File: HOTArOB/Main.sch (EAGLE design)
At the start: 15 parts

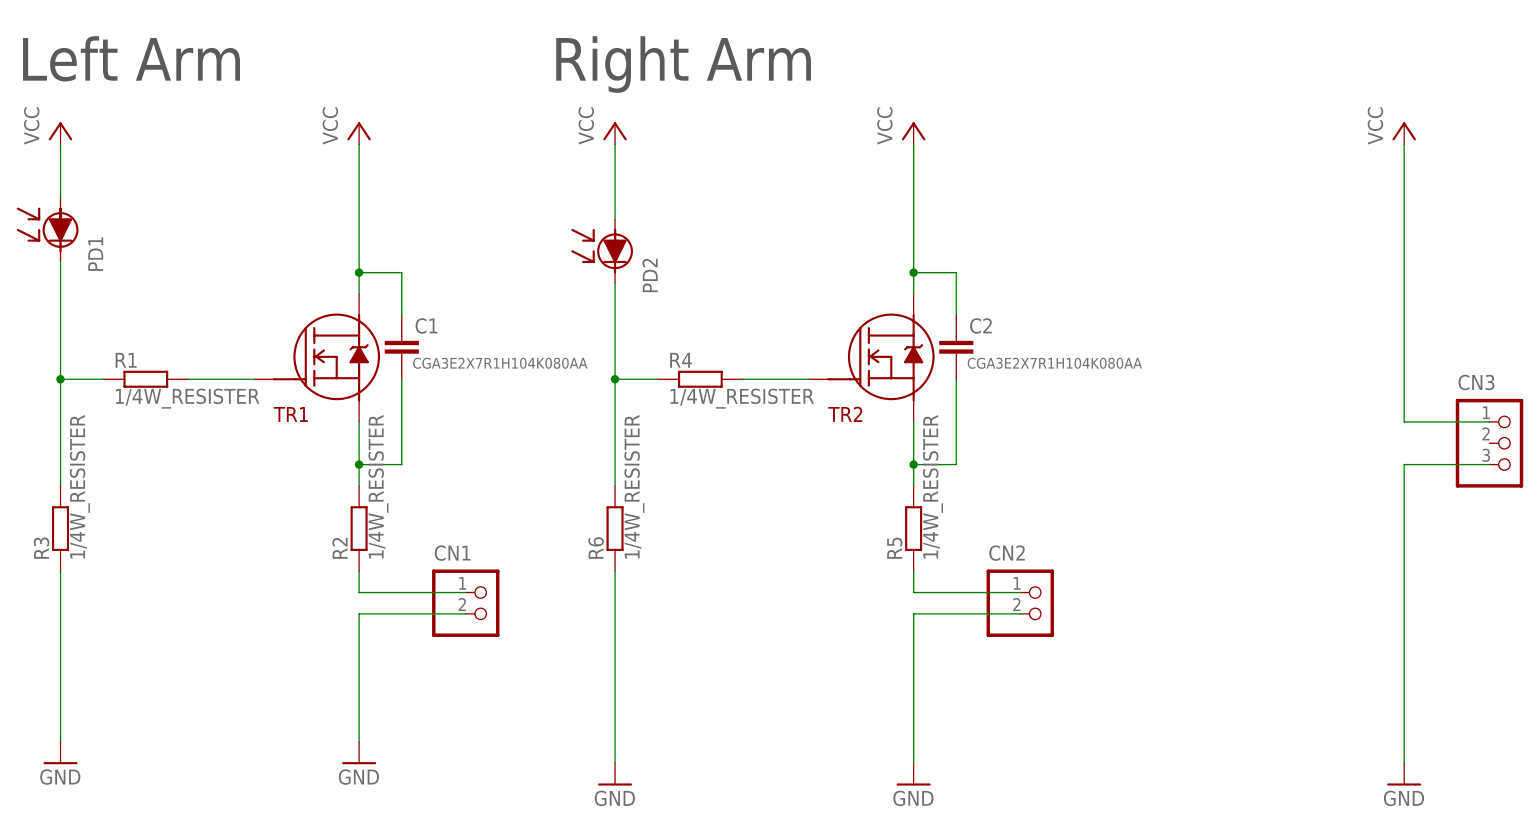
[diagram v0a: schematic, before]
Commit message: Change sensor
Photo diode to CdS
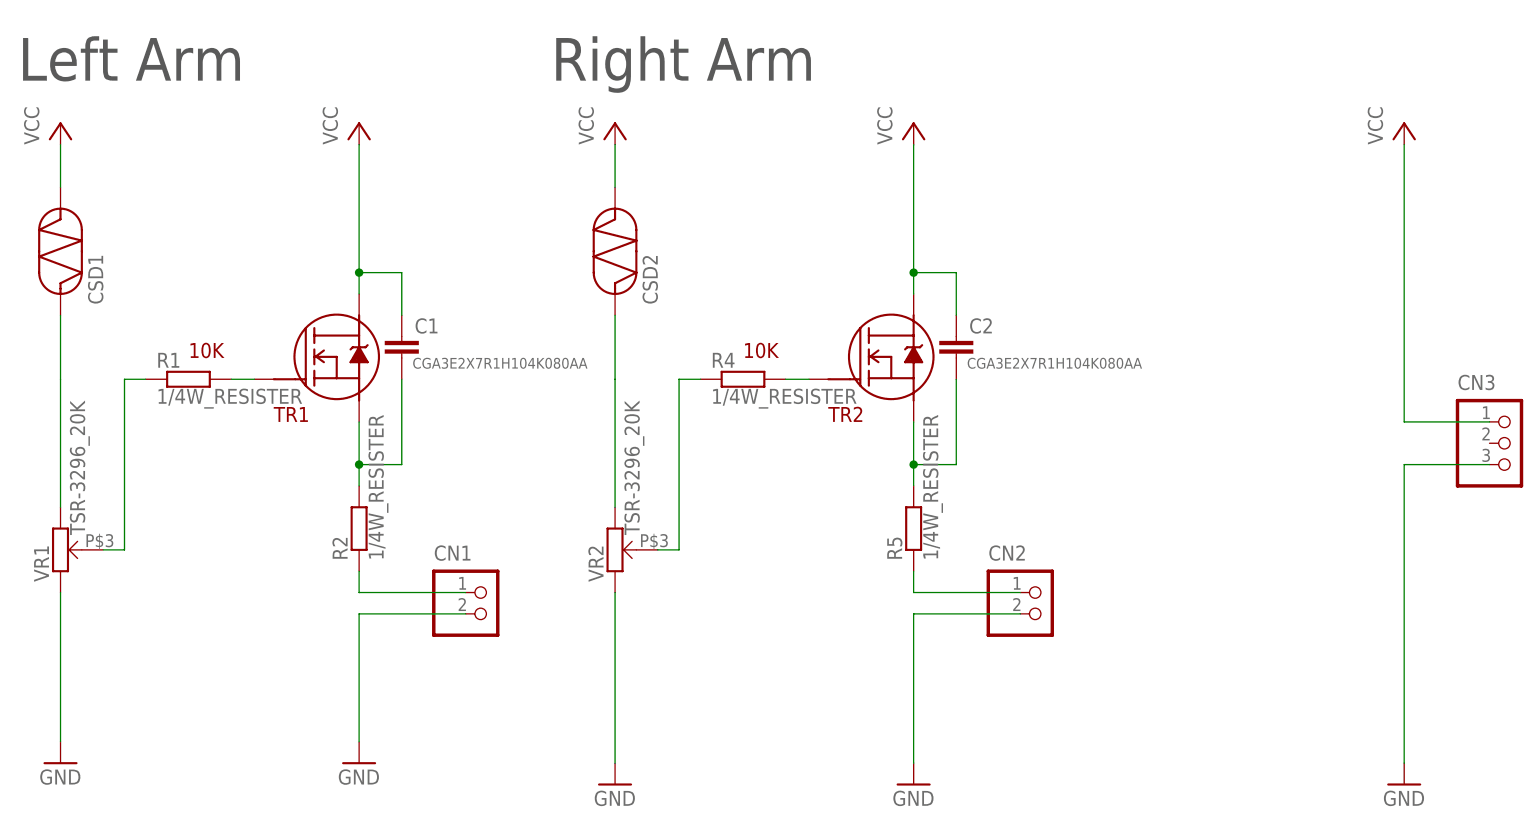
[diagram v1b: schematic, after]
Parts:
- removed PD1, PD2: LLS05-A, Tr_EXT:LLS05-A
- removed R3, R6: 1/4W_RESISTER, Tr_EXT:1/4W_RESISTER
- added CSD1, CSD2: GL5528, Tr_EXT:GL5528
- added VR1, VR2: TSR-3296_20K, Tr_EXT:TSR-3296_20K
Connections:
- new net N$10: R4.2, VR2.P$1
- new net N$9: R1.2, VR1.P$1
- net GND: now also VR1.2, VR2.2; no longer R3.2, R6.2
- net N$3: now also CSD1.P$1, VR1.1; no longer PD1.C, R1.2, R3.1
- net N$7: now also CSD2.P$1, VR2.1; no longer PD2.C, R4.2, R6.1
- net VCC: now also CSD1.P$2, CSD2.P$2; no longer PD1.A, PD2.A
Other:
- note added: "10K"
- moved on the sheet: R1, R4
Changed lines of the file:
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@@
 <part name="R1" library="Tr_EXT" deviceset="1/4W_RESISTER" device=""/>
 <part name="R2" library="Tr_EXT" deviceset="1/4W_RESISTER" device=""/>
-<part name="R3" library="Tr_EXT" deviceset="1/4W_RESISTER" device=""/>
 <part name="R5" library="Tr_EXT" deviceset="1/4W_RESISTER" device=""/>
 <part name="TR1" library="Tr_EXT" deviceset="RN5006" device=""/>
@@
 <part name="C1" library="TDK" deviceset="CGA3E2X7R1H104K080AA" device=""/>
 <part name="C2" library="TDK" deviceset="CGA3E2X7R1H104K080AA" device=""/>
-<part name="PD1" library="Tr_EXT" deviceset="LLS05-A" device=""/>
-<part name="PD2" library="Tr_EXT" deviceset="LLS05-A" device=""/>
 <part name="R4" library="Tr_EXT" deviceset="1/4W_RESISTER" device=""/>
-<part name="R6" library="Tr_EXT" deviceset="1/4W_RESISTER" device=""/>
 <part name="P+3" library="supply1" library_urn="urn:adsk.eagle:library:371" deviceset="VCC" device=""/>
 <part name="P+4" library="supply1" library_urn="urn:adsk.eagle:library:371" deviceset="VCC" device=""/>
@@
 <part name="P+5" library="supply1" library_urn="urn:adsk.eagle:library:371" deviceset="VCC" device=""/>
 <part name="GND5" library="supply1" library_urn="urn:adsk.eagle:library:371" deviceset="GND" device=""/>
+<part name="VR1" library="Tr_EXT" deviceset="TSR-3296_20K" device=""/>
+<part name="VR2" library="Tr_EXT" deviceset="TSR-3296_20K" device=""/>
+<part name="CSD1" library="Tr_EXT" deviceset="GL5528" device=""/>
+<part name="CSD2" library="Tr_EXT" deviceset="GL5528" device=""/>
 </parts>
 <sheets>
@@
 <text x="17.78" y="137.16" size="5.08" layer="97">Left Arm</text>
 <text x="81.28" y="137.16" size="5.08" layer="97">Right Arm</text>
+<text x="38.1" y="104.14" size="1.778" layer="94">10K</text>
+<text x="104.14" y="104.14" size="1.778" layer="94">10K</text>
 </plain>
 <instances>
 <instance part="FRAME1" gate="G$1" x="0" y="0"/>
-<instance part="R1" gate="G$1" x="33.02" y="101.6"/>
+<instance part="R1" gate="G$1" x="38.1" y="101.6"/>
 <instance part="R2" gate="G$1" x="58.42" y="83.82" rot="R90"/>
-<instance part="R3" gate="G$1" x="22.86" y="83.82" rot="R90"/>
 <instance part="R5" gate="G$1" x="124.46" y="83.82" rot="R90"/>
 <instance part="TR1" gate="G$1" x="55.88" y="104.14"/>
@@
 <instance part="C1" gate="G$1" x="63.5" y="106.68"/>
 <instance part="C2" gate="G$1" x="129.54" y="106.68"/>
-<instance part="PD1" gate="G$1" x="22.86" y="119.38"/>
-<instance part="PD2" gate="G$1" x="88.9" y="116.84"/>
-<instance part="R4" gate="G$1" x="99.06" y="101.6"/>
-<instance part="R6" gate="G$1" x="88.9" y="83.82" rot="R90"/>
+<instance part="R4" gate="G$1" x="104.14" y="101.6"/>
 <instance part="P+3" gate="VCC" x="88.9" y="132.08"/>
 <instance part="P+4" gate="VCC" x="22.86" y="132.08"/>
@@
 <instance part="P+5" gate="VCC" x="182.88" y="132.08"/>
 <instance part="GND5" gate="1" x="182.88" y="53.34"/>
+<instance part="VR1" gate="G$1" x="22.86" y="81.28" rot="R90"/>
+<instance part="VR2" gate="G$1" x="88.9" y="81.28" rot="R90"/>
+<instance part="CSD1" gate="G$1" x="22.86" y="116.84" rot="R90"/>
+<instance part="CSD2" gate="G$1" x="88.9" y="116.84" rot="R90"/>
 </instances>
 <busses>
@@
 <pinref part="R1" gate="G$1" pin="1"/>
 <pinref part="TR1" gate="G$1" pin="G"/>
-<wire x1="38.1" y1="101.6" x2="45.974" y2="101.6" width="0.1524" layer="91"/>
+<wire x1="43.18" y1="101.6" x2="45.974" y2="101.6" width="0.1524" layer="91"/>
 </segment>
 </net>
@@
 </segment>
 <segment>
-<pinref part="P+4" gate="VCC" pin="VCC"/>
-<pinref part="PD1" gate="G$1" pin="A"/>
-<wire x1="22.86" y1="129.54" x2="22.86" y2="123.19" width="0.1524" layer="91"/>
-</segment>
-<segment>
-<pinref part="P+3" gate="VCC" pin="VCC"/>
-<pinref part="PD2" gate="G$1" pin="A"/>
-<wire x1="88.9" y1="129.54" x2="88.9" y2="120.65" width="0.1524" layer="91"/>
-</segment>
-<segment>
 <pinref part="P+5" gate="VCC" pin="VCC"/>
 <pinref part="CN3" gate="G$1" pin="1"/>
@@
 <wire x1="182.88" y1="96.52" x2="193.04" y2="96.52" width="0.1524" layer="91"/>
 </segment>
+<segment>
+<pinref part="P+4" gate="VCC" pin="VCC"/>
+<pinref part="CSD1" gate="G$1" pin="P$2"/>
+<wire x1="22.86" y1="129.54" x2="22.86" y2="124.46" width="0.1524" layer="91"/>
+</segment>
+<segment>
+<pinref part="P+3" gate="VCC" pin="VCC"/>
+<pinref part="CSD2" gate="G$1" pin="P$2"/>
+<wire x1="88.9" y1="129.54" x2="88.9" y2="124.46" width="0.1524" layer="91"/>
+</segment>
 </net>
 <net name="N$5" class="0">
@@
 </segment>
 <segment>
-<pinref part="R3" gate="G$1" pin="2"/>
-<pinref part="GND3" gate="1" pin="GND"/>
-<wire x1="22.86" y1="78.74" x2="22.86" y2="58.42" width="0.1524" layer="91"/>
-</segment>
-<segment>
-<pinref part="R6" gate="G$1" pin="2"/>
-<pinref part="GND4" gate="1" pin="GND"/>
-<wire x1="88.9" y1="78.74" x2="88.9" y2="55.88" width="0.1524" layer="91"/>
-</segment>
-<segment>
 <pinref part="CN3" gate="G$1" pin="3"/>
 <pinref part="GND5" gate="1" pin="GND"/>
@@
 <wire x1="182.88" y1="91.44" x2="182.88" y2="55.88" width="0.1524" layer="91"/>
 </segment>
+<segment>
+<pinref part="VR1" gate="G$1" pin="2"/>
+<pinref part="GND3" gate="1" pin="GND"/>
+<wire x1="22.86" y1="76.2" x2="22.86" y2="58.42" width="0.1524" layer="91"/>
+</segment>
+<segment>
+<pinref part="GND4" gate="1" pin="GND"/>
+<pinref part="VR2" gate="G$1" pin="2"/>
+<wire x1="88.9" y1="55.88" x2="88.9" y2="76.2" width="0.1524" layer="91"/>
+</segment>
 </net>
 <net name="N$3" class="0">
 <segment>
-<pinref part="PD1" gate="G$1" pin="C"/>
-<pinref part="R3" gate="G$1" pin="1"/>
-<wire x1="22.86" y1="115.57" x2="22.86" y2="101.6" width="0.1524" layer="91"/>
-<pinref part="R1" gate="G$1" pin="2"/>
-<wire x1="22.86" y1="101.6" x2="22.86" y2="88.9" width="0.1524" layer="91"/>
-<wire x1="27.94" y1="101.6" x2="22.86" y2="101.6" width="0.1524" layer="91"/>
-<junction x="22.86" y="101.6"/>
+<pinref part="CSD1" gate="G$1" pin="P$1"/>
+<wire x1="22.86" y1="109.22" x2="22.86" y2="101.6" width="0.1524" layer="91"/>
+<pinref part="VR1" gate="G$1" pin="1"/>
+<wire x1="22.86" y1="101.6" x2="22.86" y2="86.36" width="0.1524" layer="91"/>
 </segment>
 </net>
 <net name="N$7" class="0">
 <segment>
-<pinref part="PD2" gate="G$1" pin="C"/>
-<pinref part="R6" gate="G$1" pin="1"/>
-<wire x1="88.9" y1="113.03" x2="88.9" y2="101.6" width="0.1524" layer="91"/>
-<pinref part="R4" gate="G$1" pin="2"/>
-<wire x1="88.9" y1="101.6" x2="88.9" y2="88.9" width="0.1524" layer="91"/>
-<wire x1="93.98" y1="101.6" x2="88.9" y2="101.6" width="0.1524" layer="91"/>
-<junction x="88.9" y="101.6"/>
+<pinref part="VR2" gate="G$1" pin="1"/>
+<wire x1="88.9" y1="86.36" x2="88.9" y2="101.6" width="0.1524" layer="91"/>
+<pinref part="CSD2" gate="G$1" pin="P$1"/>
+<wire x1="88.9" y1="101.6" x2="88.9" y2="109.22" width="0.1524" layer="91"/>
 </segment>
 </net>
@@
 <pinref part="R4" gate="G$1" pin="1"/>
 <pinref part="TR2" gate="G$1" pin="G"/>
-<wire x1="104.14" y1="101.6" x2="112.014" y2="101.6" width="0.1524" layer="91"/>
-</segment>
-</net>
+<wire x1="109.22" y1="101.6" x2="112.014" y2="101.6" width="0.1524" layer="91"/>
+</segment>
+</net>
+<net name="N$9" class="0">
+<segment>
+<pinref part="VR1" gate="G$1" pin="P$1"/>
+<wire x1="27.94" y1="81.28" x2="30.48" y2="81.28" width="0.1524" layer="91"/>
+<pinref part="R1" gate="G$1" pin="2"/>
+<wire x1="30.48" y1="81.28" x2="30.48" y2="101.6" width="0.1524" layer="91"/>
+<wire x1="30.48" y1="101.6" x2="33.02" y2="101.6" width="0.1524" layer="91"/>
+</segment>
+</net>
+<net name="N$10" class="0">
+<segment>
+<pinref part="VR2" gate="G$1" pin="P$1"/>
+<wire x1="93.98" y1="81.28" x2="96.52" y2="81.28" width="0.1524" layer="91"/>
+<pinref part="R4" gate="G$1" pin="2"/>
+<wire x1="96.52" y1="81.28" x2="96.52" y2="101.6" width="0.1524" layer="91"/>
+<wire x1="96.52" y1="101.6" x2="99.06" y2="101.6" width="0.1524" layer="91"/>
+</segment>
+</net>

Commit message: working commit
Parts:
- removed R4, R5: 1/4W_RESISTER, Tr_EXT:1/4W_RESISTER
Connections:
- removed net N$10: R4.2, VR2.P$1
- removed net N$5: CN1.1, R2.2
- removed net N$6: CN2.1, R5.2
- removed net N$7: CSD2.P$1, VR2.1
- net GND: now also R1.2, R2.2; no longer CN1.2, CN2.2
- net N$1: now also C1.1, CN1.2, TR1.D; no longer R1.1, TR1.G
- net N$2: now also R1.1; no longer R2.1
- net N$3: now also C2.1, CN2.2, TR2.D; no longer CSD1.P$1, VR1.1
- net N$4: now also R2.1; no longer R5.1
- net N$8: now also CSD2.P$1, VR2.P$1; no longer R4.1
- net N$9: now also CSD1.P$1, TR1.G; no longer R1.2
- net VCC: now also CN1.1, CN2.1; no longer C1.1, C2.1, TR1.D, TR2.D
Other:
- moved on the sheet: CN1, CN2, R1, R2
